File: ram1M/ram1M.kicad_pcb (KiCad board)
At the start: 2 copper layers, 108.6 x 24.3 mm, 7 parts, among them J1 ramslot, U1 74HC32, U2 AS6C4008-55PCN, U3 AS6C4008-55PCN

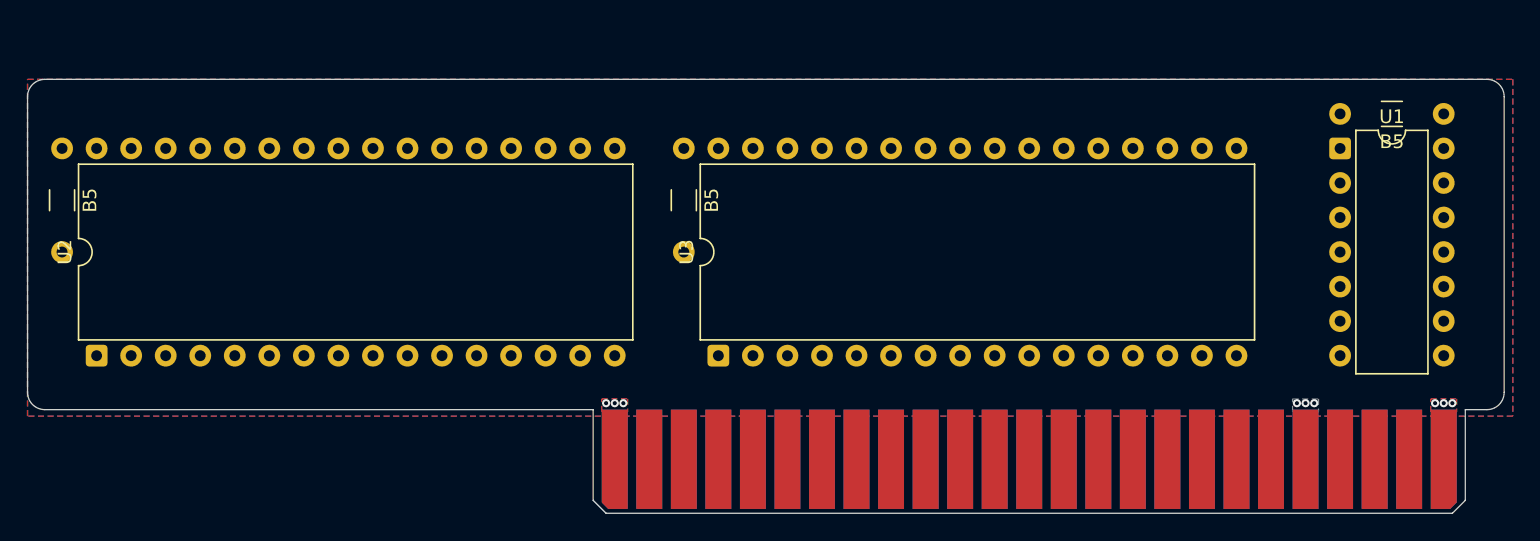
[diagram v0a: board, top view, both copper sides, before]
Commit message: [ram1M] restored from a SF68 backup
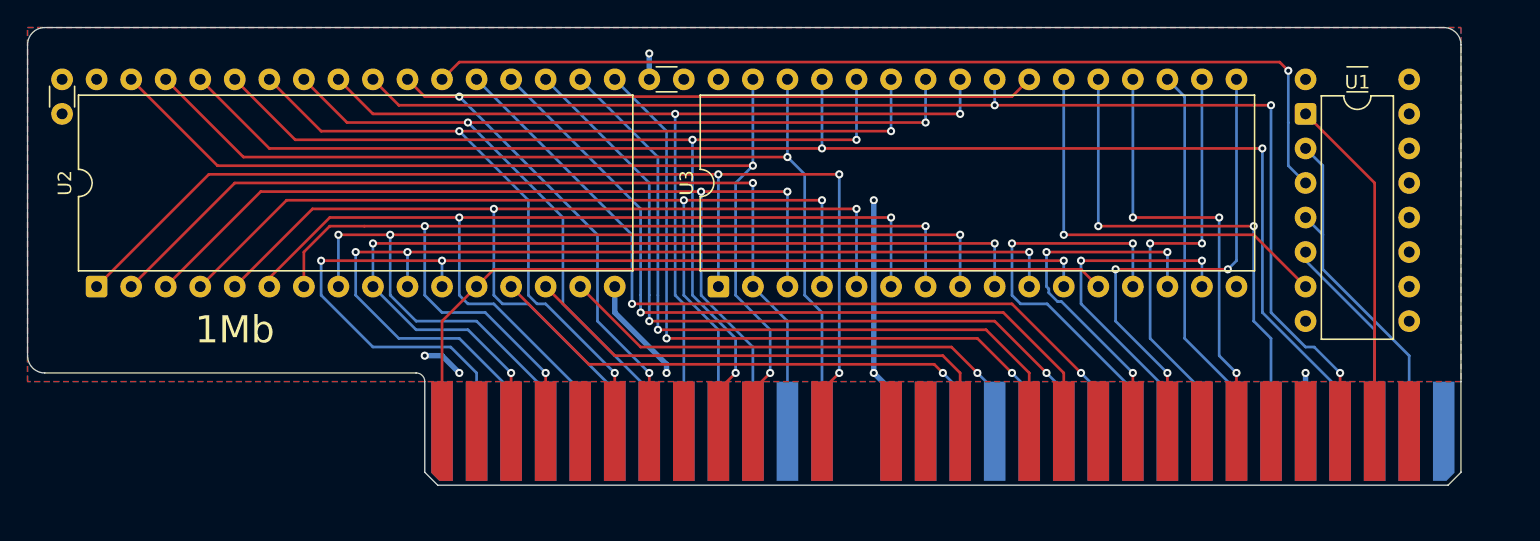
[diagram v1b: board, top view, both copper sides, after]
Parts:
- removed B5 (x3): C_Disc_D3.0mm_W1.6mm_P7.62mm, Capacitor_THT:C_Disc_D3.0mm_W1.6mm_P7.62mm
- removed J1: ramslot, Connector_PCBEdge:pcb_edge_50_P2.54
- added CB1: C_Disc_D3.0mm_W1.6mm_P2.54mm, Capacitor_THT:C_Disc_D3.0mm_W1.6mm_P2.54mm, F.Cu at (203.2, 48.3)
- added CB1: C_Disc_D3.0mm_W1.6mm_P7.62mm, Capacitor_THT:C_Disc_D3.0mm_W1.6mm_P7.62mm, F.Cu at (256.5, 48.3)
- added CB1: C_Disc_D3.0mm_W1.6mm_P2.54mm, Capacitor_THT:C_Disc_D3.0mm_W1.6mm_P2.54mm, F.Cu at (157.5, 48.3)
- added J5: ramslot, Connector_PCBEdge:pcb_edge_60_P2.54_new, F.Cu at (184.2, 70.5)
- moved U2 5.08 mm to (160.0, 63.5)
- moved U3 5.08 mm to (205.7, 63.5)
- moved U1 3.59 mm to (248.9, 50.8)
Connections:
- net /PDIR.~{R} renamed /DIR.~{R}
- net /PDIR.~{W} renamed /DIR.~{W}
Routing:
- net /DIR.~{W}: track 0.00 -> 108.5 mm, vias 0 -> 2
- net /DIR.~{R}: track 0.00 -> 95.8 mm, vias 0 -> 3
- net /A_{19}: track 0.00 -> 85.7 mm, vias 0 -> 3
- net /A_{2}: track 0.00 -> 79.0 mm, vias 0 -> 3
- net /A_{10}: track 0.00 -> 78.4 mm, vias 0 -> 2
- net /A_{9}: track 0.00 -> 78.3 mm, vias 0 -> 3
- net /A_{11}: track 0.00 -> 77.2 mm, vias 0 -> 2
- net /A_{16}: track 0.00 -> 76.3 mm, vias 0 -> 2
- net /A_{14}: track 0.00 -> 75.3 mm, vias 0 -> 3
- net /A_{5}: track 0.00 -> 75.1 mm, vias 0 -> 3
- net /A_{3}: track 0.00 -> 75.1 mm, vias 0 -> 3
- net /A_{18}: track 0.00 -> 75.0 mm, vias 0 -> 1
- net /A_{8}: track 0.00 -> 75.0 mm, vias 0 -> 2
- net /A_{15}: track 0.00 -> 74.8 mm, vias 0 -> 2
- net /A_{6}: track 0.00 -> 74.1 mm, vias 0 -> 3
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- removed copper zone on F.Cu, net +5V
- removed copper zone on B.Cu, net GND
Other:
- board size 108.6 x 24.3 mm -> 105.4 x 26 mm
- board text added: "1Mb"
